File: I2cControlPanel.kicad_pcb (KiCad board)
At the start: 2 copper layers, 100 x 100 mm, 61 parts, among them J1 JoystickL, J2 Conn_01x06, J3 Conn_01x04, J4 Conn_01x04, J5 JoystickR, J6 Conn_01x04, SW6 SW_Push, U1 NJM12888F33, U2 ATmega328PB-MU, U3 AQM0802

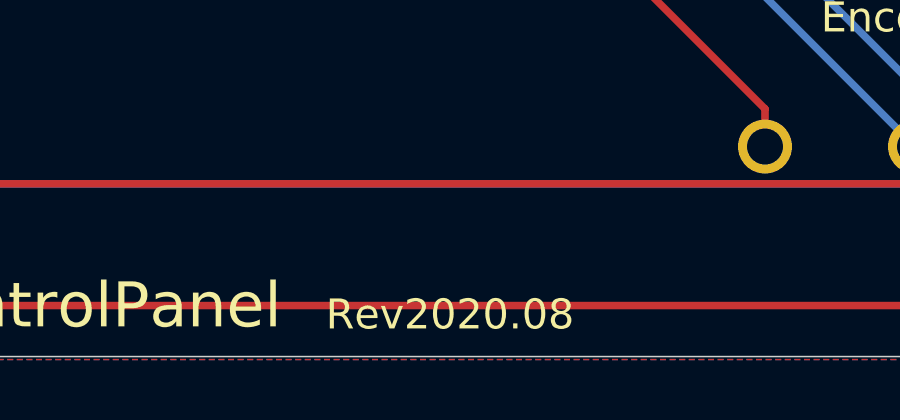
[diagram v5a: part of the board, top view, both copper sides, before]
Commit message: Update revision to 2020.08 and github url and arduino library info
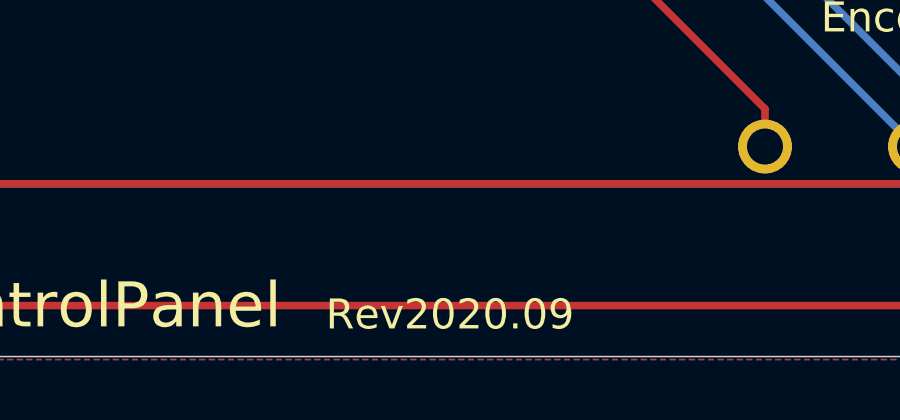
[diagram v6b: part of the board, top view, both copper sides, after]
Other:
- board text added: "PCB info: https://github.com/asukiaaa/I2cControlPanel Arduino library: I2cControlPanel_asukiaaa"
- board text added: "Rev2020.09"
- board text removed: "Rev2020.08"

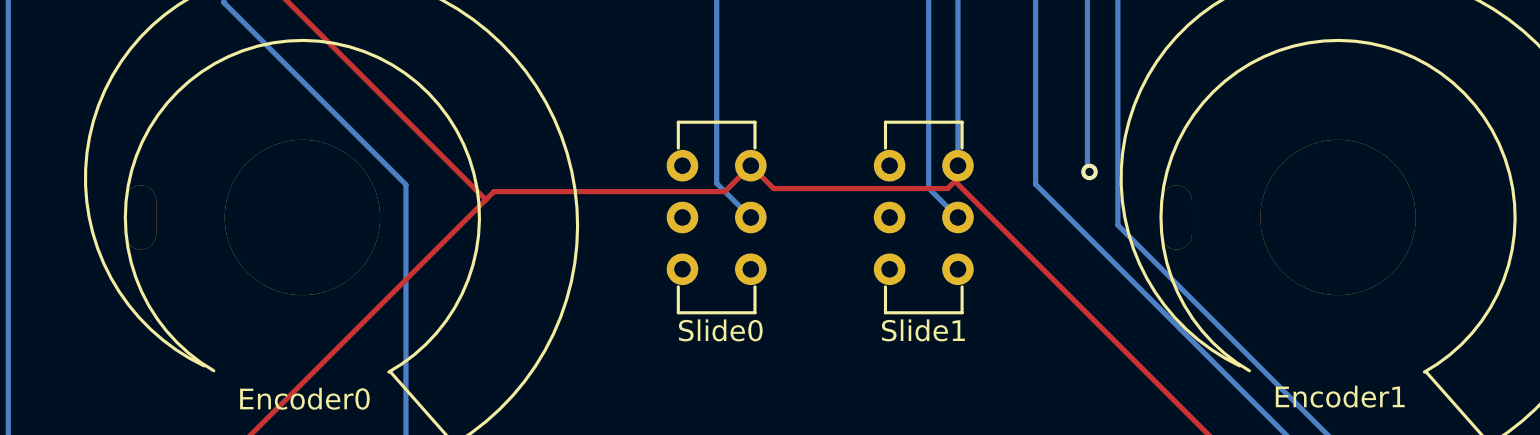
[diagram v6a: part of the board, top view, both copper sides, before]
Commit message: Update hole position of volume
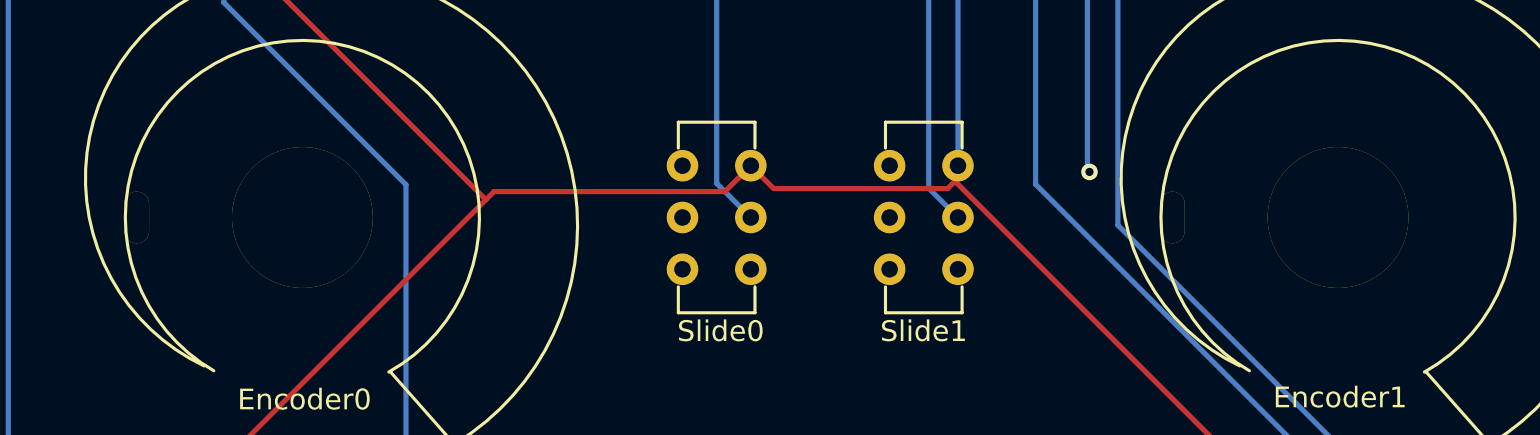
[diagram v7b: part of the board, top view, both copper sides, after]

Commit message: Replace vert and hori for joy
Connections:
- J1 pad 2: /VertValueL -> /HoriValueL
- J1 pad 5: /HoriValueL -> /VertValueL
- J5 pad 2: /HoriValueR -> /VertValueR
- J5 pad 5: /VertValueR -> /HoriValueR
- U2 pad 23: /HoriValueL -> /VertValueL
- U2 pad 24: /VertValueL -> /HoriValueL
- U2 pad 25: /HoriValueR -> /VertValueR
- U2 pad 26: /VertValueR -> /HoriValueR
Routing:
- net /VertValueL: track 25.9 -> 35.9 mm
- net /HoriValueL: track 35.9 -> 25.9 mm
- net /VertValueR: track 28.2 -> 32.3 mm
- net /HoriValueR: track 32.3 -> 28.2 mm
